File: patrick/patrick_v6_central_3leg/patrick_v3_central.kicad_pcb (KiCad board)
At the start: 2 copper layers, 47.6 x 51.7 mm, 27 parts, among them J1 Conn_02x05_Counter_Clockwise, J10 61300311121, J4 Conn_02x05_Counter_Clockwise, J5 Conn_02x05_Counter_Clockwise, J7 61300211121, J9 61300211121, Q1 RUE002N02TL, Q2 RUE002N02TL, Q3 RUE002N02TL, U1 MPM3610GQV-Z, U2 ICM-20948, U3 BL652-SA-01, U4 MCP1703T-1802E_CB

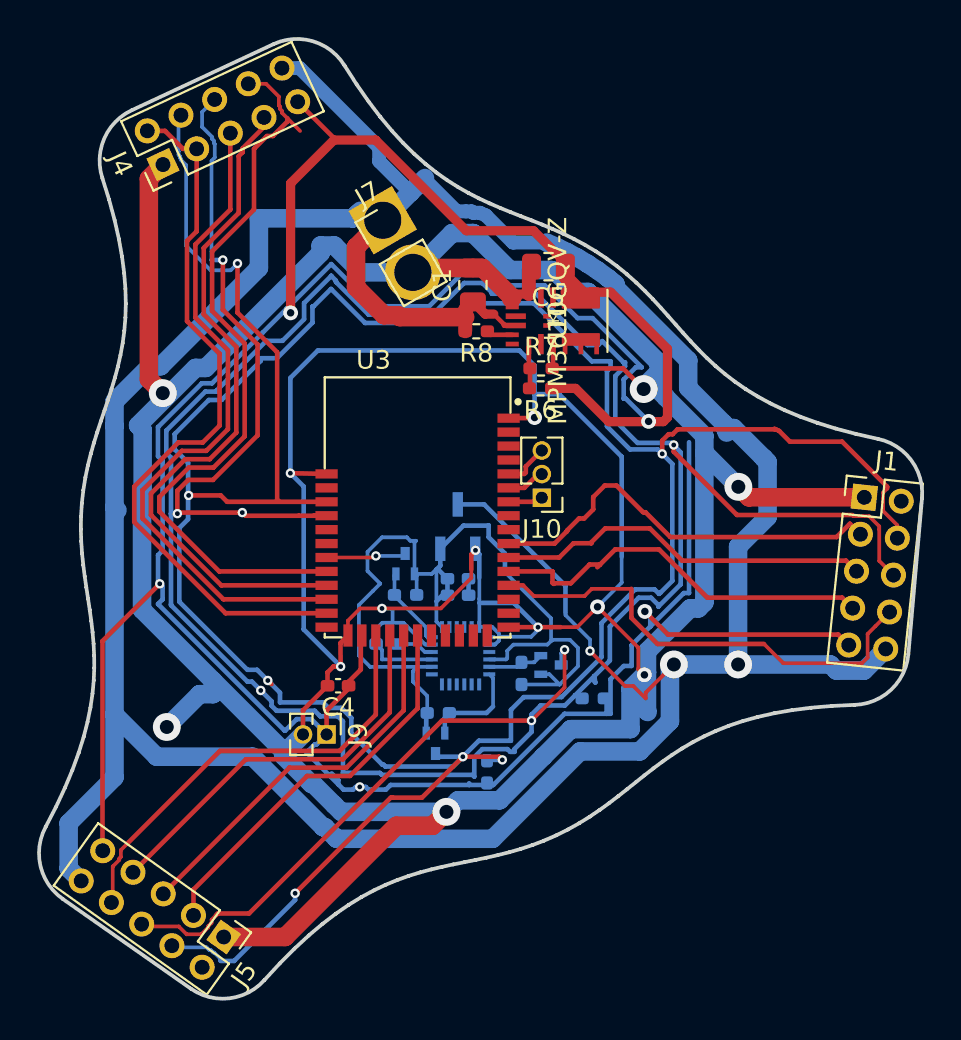
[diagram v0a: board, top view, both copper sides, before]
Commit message: separate gnd
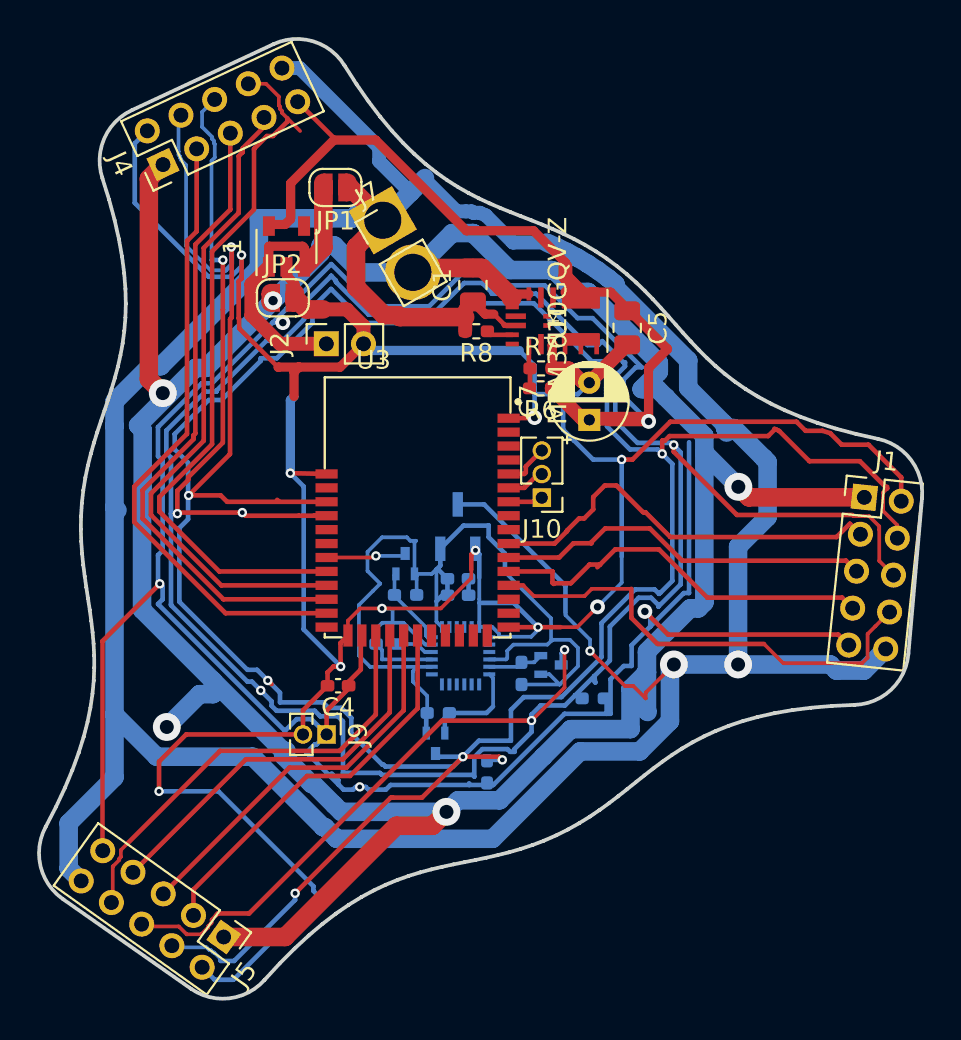
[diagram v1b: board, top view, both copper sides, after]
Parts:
- added 1: V_REG_SPX3819-SOT23-5, Package_TO_SOT_SMD:SOT-23-5, F.Cu at (101.8, 94.5)
- added C7: CP1_Small, Capacitor_THT:CP_Radial_D4.0mm_P2.00mm, F.Cu at (118.1, 103.8)
- added J2: Conn_01x02, Connector_PinSocket_2.00mm:PinSocket_1x02_P2.00mm_Vertical, F.Cu at (103.9, 99.7)
- added JP1: Jumper_NO_Small, Jumper:SolderJumper-2_P1.3mm_Open_RoundedPad1.0x1.5mm, F.Cu at (104.4, 91.3)
- added JP2: Jumper_NO_Small, Jumper:SolderJumper-2_P1.3mm_Open_RoundedPad1.0x1.5mm, F.Cu at (101.6, 97.3)
- moved C5 5.37 mm to (120.1, 98.9), turned to 270 degrees
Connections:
- C2 pad 1: GND -> GND2
- C3 pad 1: GND -> GND2
- C4 pad 2: GND -> GND2
- C5 pad 2: GND -> GND2
- C6 pad 1: GND -> GND2
- J1 pad 2: Net-(J1-Pad2) -> GND2
- J4 pad 2: /SMA4_SIG -> GND2
- J5 pad 2: Net-(J5-Pad2) -> GND2
- J9 pad 2: GND -> GND2
- R7 pad 2: GND -> GND2
- U1 pad 3: GND -> GND2
- U2 pad 11: GND -> GND2
- U2 pad 18: GND -> GND2
- U2 pad 20: GND -> Net-(U2-Pad20)
- U2 pad 9: GND -> GND2
- U3 pad 1: GND -> GND2
- U3 pad 16: GND -> GND2
- U3 pad 27: GND -> GND2
- U3 pad 39: GND -> GND2
- U4 pad 1: GND -> GND2
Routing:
- net GND2: track 0.00 -> 180.7 mm, vias 0 -> 10
- net GND: track 265.4 -> 154.8 mm, vias 13 -> 5
- net Net-(1-Pad1): track 0.00 -> 16.4 mm
- net /SMA4_SIG: track 39.2 -> 33.9 mm
- net +8V: track 181.6 -> 184.3 mm
- net /+3V: track 183.3 -> 180.8 mm
- net /SCL: track 181.6 -> 179.2 mm
- net /SMA1_SIG: track 41.1 -> 38.8 mm
- net /SMA3_SIG: track 36.6 -> 34.4 mm
- net /SMA2_SIG: track 37.2 -> 35.0 mm
- net /SDA: track 166.3 -> 167.8 mm
